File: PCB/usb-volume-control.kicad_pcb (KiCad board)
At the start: 2 copper layers, 55.9 x 57.8 mm, 17 parts, among them P201 ROT ENC

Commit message: Improved PCB layout
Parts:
- added Rc303: 2k, Resistors_SMD:R_0805_HandSoldering, F.Cu at (141.6, 96.5)
- P201, Pc101: footprint Pin_Headers:Pin_Header_Straight_1x05 -> Pin_Headers:Pin_Header_Straight_1x04
- moved Rc201 42.3 mm to (140.3, 148.6), turned to 270 degrees
- moved Dc201 33.3 mm to (140.3, 143.5), turned to 90 degrees
- moved Rc202 31.8 mm to (135.3, 148.6), turned to 270 degrees
- moved Dc202 30.7 mm to (135.3, 143.5), turned to 90 degrees
- moved Pc101 23.6 mm to (148.0, 142.2), turned to 0 degrees
- moved P201 16.1 mm to (139.7, 90.8), turned to 90 degrees
- moved Rc101 10.3 mm to (153.7, 141.6), turned to 0 degrees
- moved Cc302 1.80 mm to (132.7, 108.6)
- moved Rc102 1.80 mm to (141.0, 103.5)
- moved Uc101 1.80 mm to (147.2, 103.7)
- moved Cc101 1.80 mm to (132.7, 122.6)
- moved Cc102 1.80 mm to (132.7, 127.6)
- moved Cc301 1.80 mm to (132.7, 102.2)
- moved Cp101 1.80 mm to (141.6, 116.2)
- moved Rc301 1.80 mm to (132.7, 95.9)
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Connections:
- Pc101 pad 4: Net-(Pc101-Pad4) -> GND
- Uc101 pad 28: Net-(Uc101-Pad28) -> Net-(P201-Pad4)
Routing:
- net Net-(Dc202-Pad1): track 23.5 -> 61.7 mm
- net VCC: track 133.9 -> 97.7 mm, vias 2 -> 0
- net Net-(Dc201-Pad1): track 80.9 -> 44.9 mm, vias 3 -> 2
- net Net-(P201-Pad4): track 0.00 -> 23.2 mm
- net Net-(Pc101-Pad3): track 13.7 -> 35.1 mm
- net Net-(Cc302-Pad1): track 41.2 -> 60.9 mm
- net GND: track 177.0 -> 157.4 mm, vias 2 -> 5
- net Net-(Cc301-Pad1): track 34.8 -> 42.7 mm
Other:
- board size 55.9 x 57.8 mm -> 33 x 73.7 mm

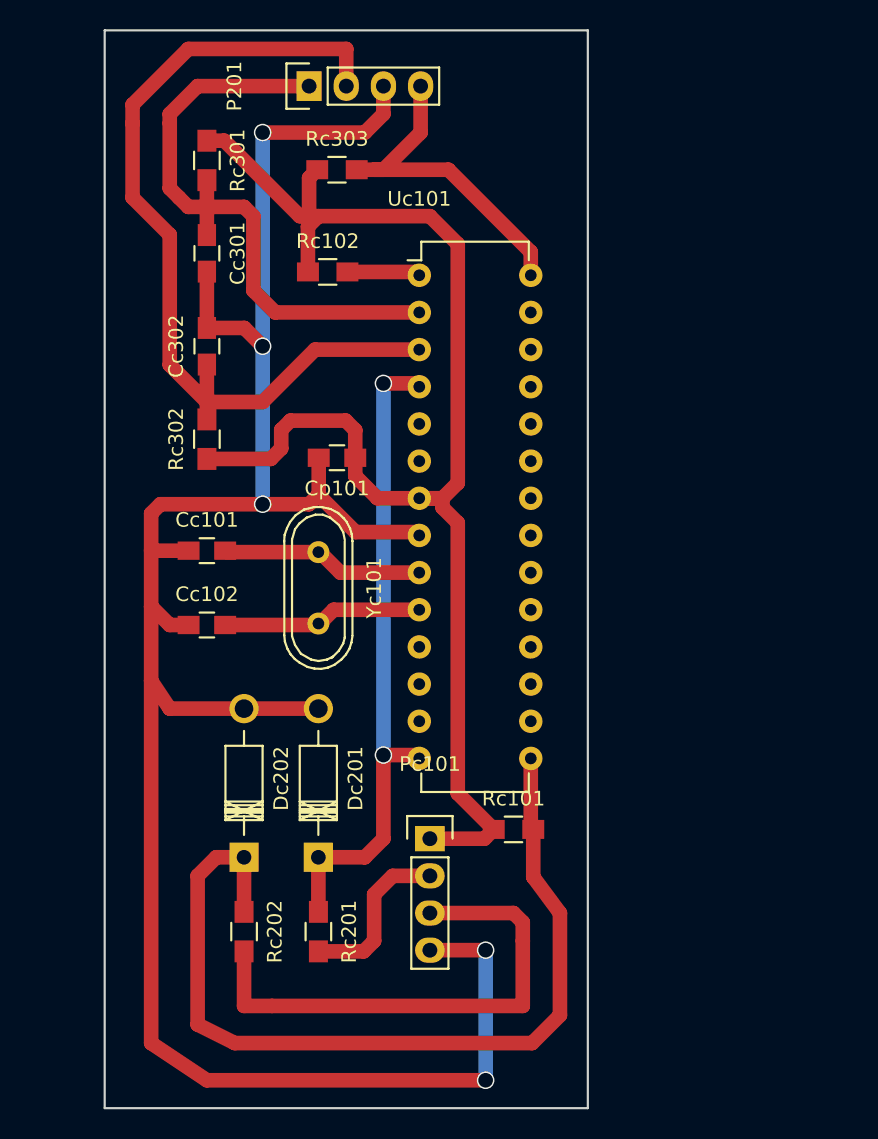
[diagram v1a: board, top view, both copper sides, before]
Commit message: Fixed connection error
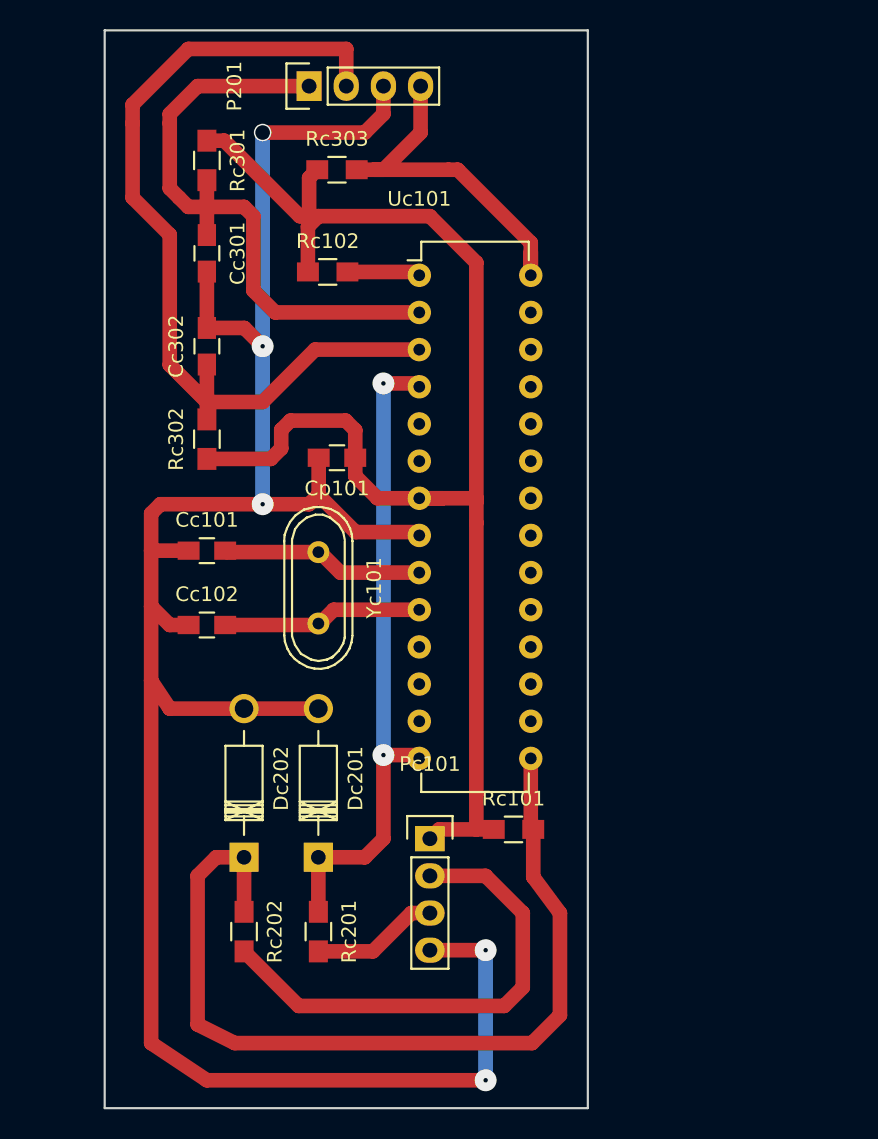
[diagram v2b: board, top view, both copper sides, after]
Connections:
- Rc201 pad 2: Net-(Pc101-Pad2) -> Net-(Pc101-Pad3)
- Rc202 pad 2: Net-(Pc101-Pad3) -> Net-(Pc101-Pad2)
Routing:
- net Net-(Pc101-Pad3): track 35.1 -> 8.71 mm
- net Net-(Pc101-Pad2): track 11.6 -> 33.6 mm
- net Net-(P201-Pad4): track 23.2 -> 25.2 mm
- net VCC: track 97.7 -> 99.1 mm
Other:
- net class Default: via_dia 1.2 -> 1.5; via_drill 1 -> 0.3

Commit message: Changed rotary encoder capacitor value
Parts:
- Cc301, Cc302: value 10uF -> 1uF
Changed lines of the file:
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@@
       (effects (font (size 1 1) (thickness 0.15)))
     )
-    (fp_text value 10uF (at 0 2.1 270) (layer F.Fab)
+    (fp_text value 1uF (at 0 2.1 270) (layer F.Fab)
       (effects (font (size 1 1) (thickness 0.15)))
     )
@@
       (effects (font (size 1 1) (thickness 0.15)))
     )
-    (fp_text value 10uF (at 0 2.1 90) (layer F.Fab)
+    (fp_text value 1uF (at 0 2.1 90) (layer F.Fab)
       (effects (font (size 1 1) (thickness 0.15)))
     )
@@
   (segment (start 142.955 96.52) (end 144.145 96.52) (width 1) (layer F.Cu) (net 27))
   (segment (start 154.8511 102.1461) (end 154.8511 103.7336) (width 1) (layer F.Cu) (net 27))
-  (segment (start 147.955 144.78) (end 151.765 144.78) (width 1) (layer F.Cu) (net 28) (status 400000))
-  (segment (start 138.985 153.67) (end 135.255 149.94) (width 1) (layer F.Cu) (net 28) (status 800000))
+  (segment (start 147.955 144.78) (end 151.765 144.78) (width 1) (layer F.Cu) (net 28))
+  (segment (start 138.985 153.67) (end 135.255 149.94) (width 1) (layer F.Cu) (net 28))
   (segment (start 153.035 153.67) (end 138.985 153.67) (width 1) (layer F.Cu) (net 28))
   (segment (start 154.305 152.4) (end 153.035 153.67) (width 1) (layer F.Cu) (net 28))
   (segment (start 154.305 147.32) (end 154.305 152.4) (width 1) (layer F.Cu) (net 28))
   (segment (start 151.765 144.78) (end 154.305 147.32) (width 1) (layer F.Cu) (net 28))
-  (segment (start 147.955 147.32) (end 146.685 147.32) (width 1) (layer F.Cu) (net 29) (status 400000))
-  (segment (start 144.065 149.94) (end 140.335 149.94) (width 1) (layer F.Cu) (net 29) (status 800000))
+  (segment (start 147.955 147.32) (end 146.685 147.32) (width 1) (layer F.Cu) (net 29))
+  (segment (start 144.065 149.94) (end 140.335 149.94) (width 1) (layer F.Cu) (net 29))
   (segment (start 146.685 147.32) (end 144.065 149.94) (width 1) (layer F.Cu) (net 29))
 )
